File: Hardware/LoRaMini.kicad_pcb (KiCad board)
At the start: 2 copper layers, 89.3 x 39.2 mm, 65 parts, among them J2 Conn_01x01_Female, J3 USB4125-GF-A_REVA2, Q1 Q_PMOS_GSD, Q2 Q_NMOS_GSD, U1 BQ25060, U2 NCP170ASN330T2G_, U3 STM32G071KxU, U4 RFM95W-868S2, Y1 32KHz

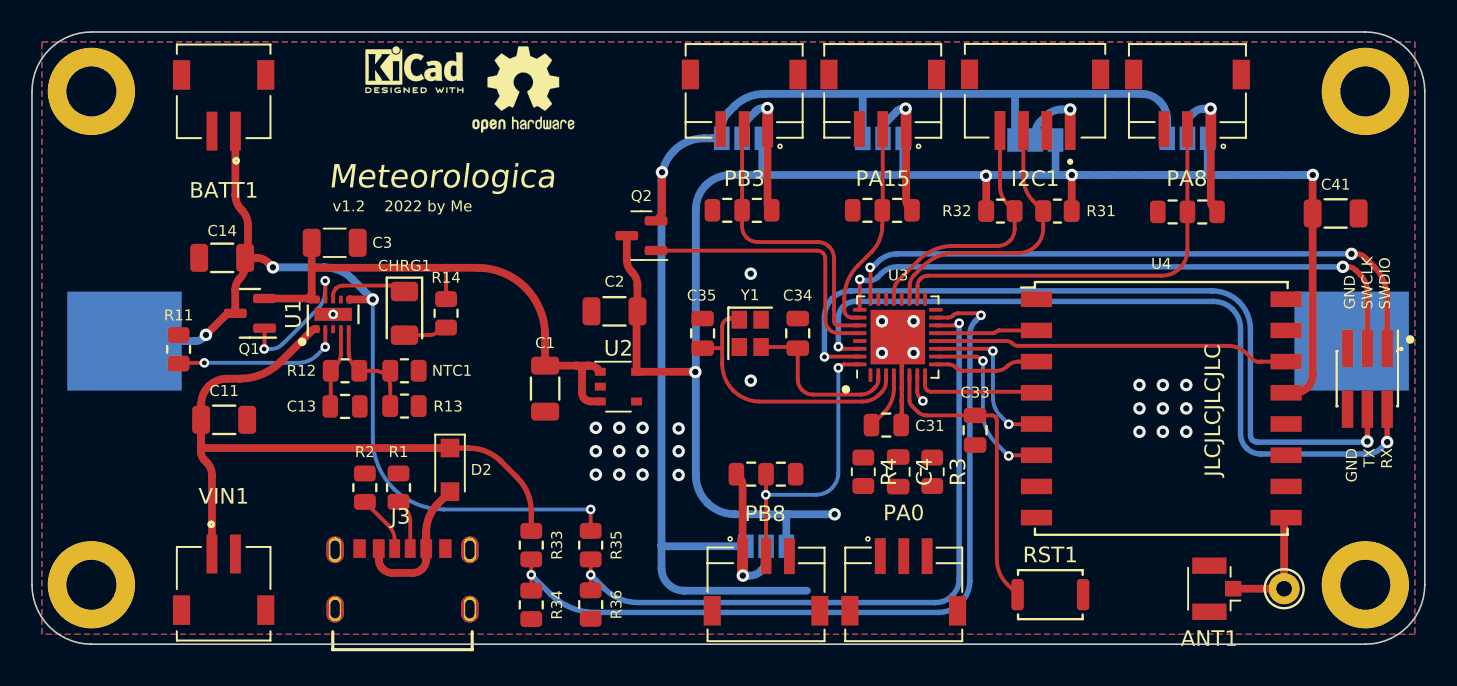
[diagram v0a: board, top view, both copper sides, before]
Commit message: fixed PA0
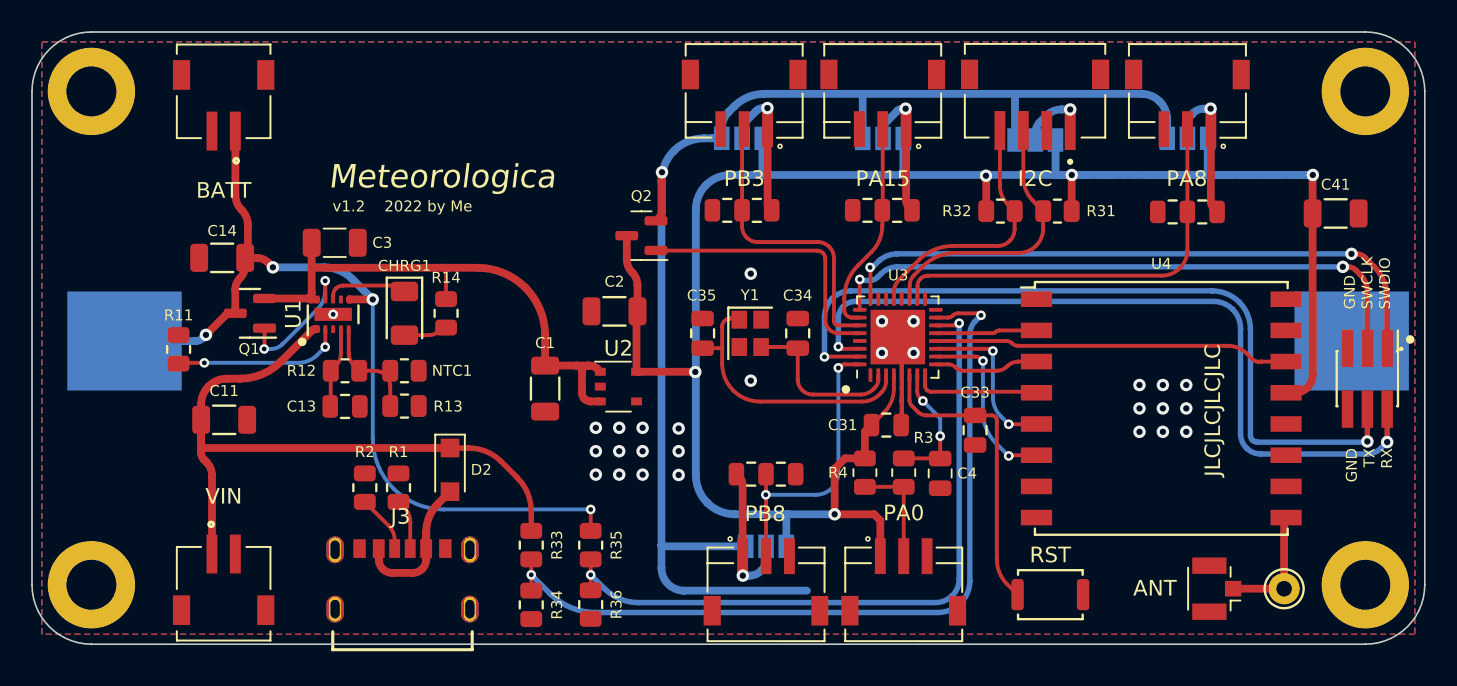
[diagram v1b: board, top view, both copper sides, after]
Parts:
- removed the REF** at (123.4, 104.3)
- removed the REF** at (116.5, 103.0)
- moved C4 2.69 mm to (150.2, 128.9)
- moved R3 1.83 mm to (147.8, 128.8)
- moved R4 0.11 mm to (145.3, 128.8)
- renumbered ANT1 to ANT, BATT1 to BATT, I2C1 to I2C, RST1 to RST, VIN1 to VIN
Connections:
- PA0 pad 1: unconnected-(PA0-Pad1) -> +3V3
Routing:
- net +3V3: track 115.8 -> 128.6 mm
- net Net-(PA0-Pad2): track 0.00 -> 6.93 mm
- net PA0: track 1.77 -> 8.27 mm, vias 1 -> 2
